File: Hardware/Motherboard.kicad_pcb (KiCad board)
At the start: 2 copper layers, 130 x 81.3 mm, 54 parts, among them J1 BME680, J2 JTAG, J3 Display_1, J4 Display_2, J5 Buttons, J6 USB, J7 MUSBD111M0_Supply, Q1 DMG3414U, SW1 Button_Plus, SW2 Button_Minus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

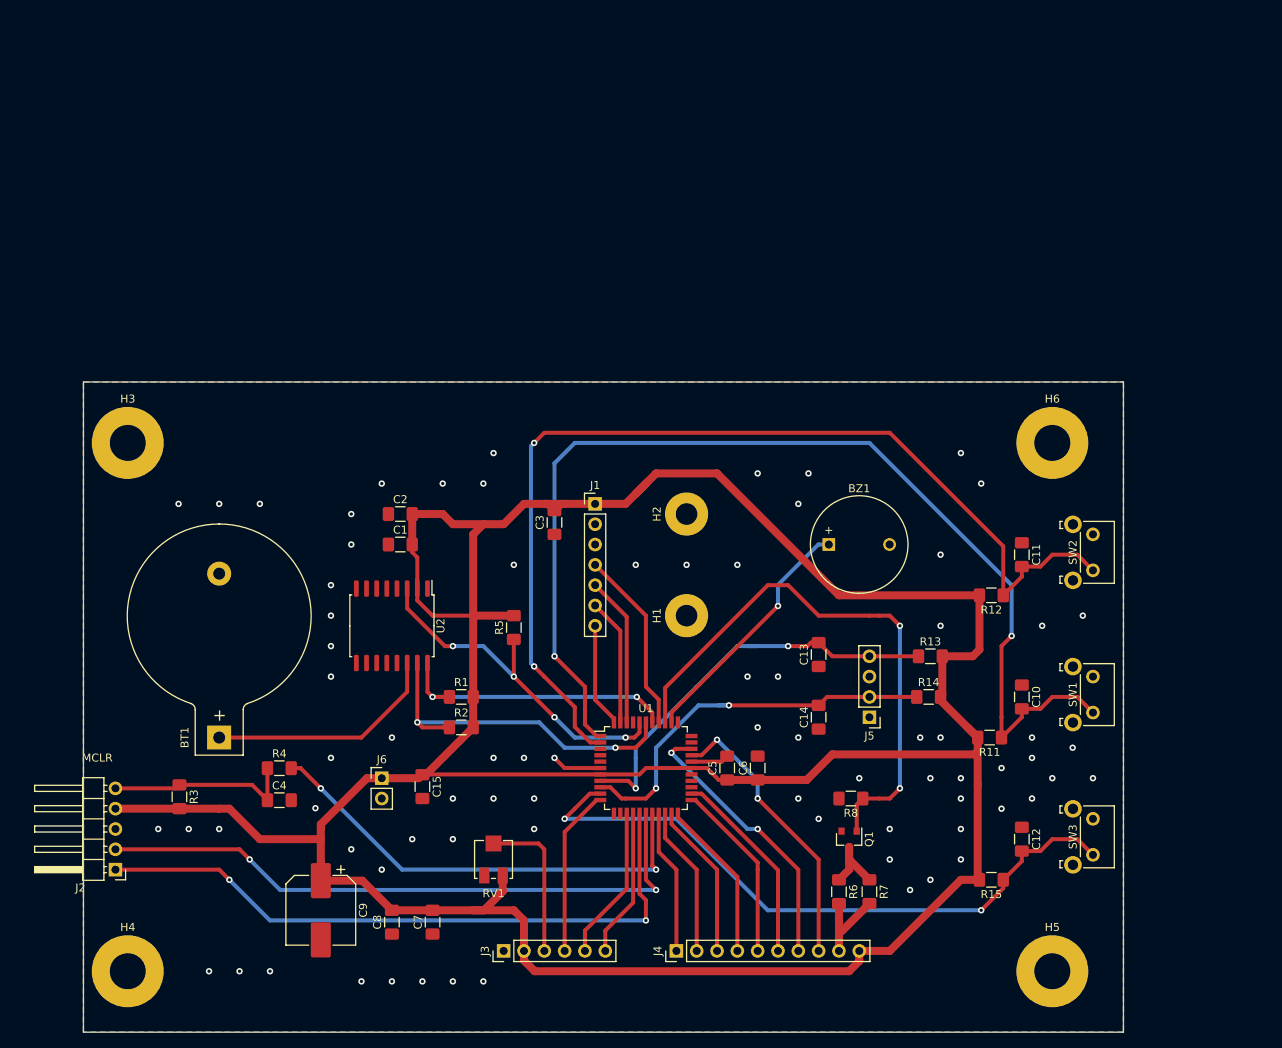
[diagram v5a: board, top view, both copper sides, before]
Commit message: [Hardware] Slightly decreased PCB height and adjusted it to millimeters.
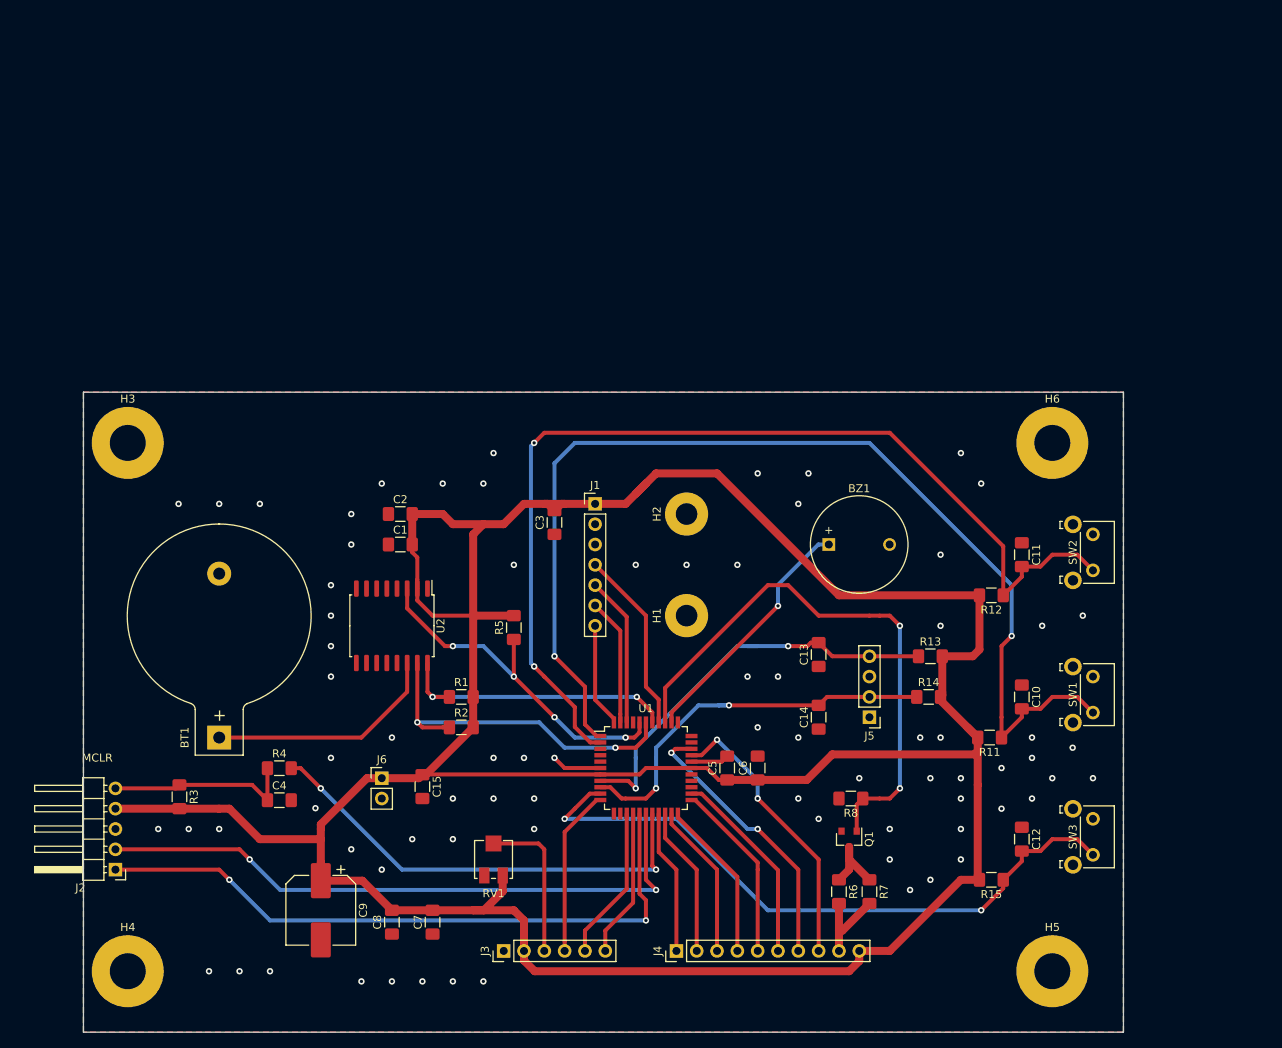
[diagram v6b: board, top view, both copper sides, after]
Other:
- board size 130 x 81.3 mm -> 130 x 80 mm
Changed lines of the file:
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@@
   (general
     (thickness 1.6)
-    (drawings 7)
+    (drawings 8)
     (tracks 463)
     (zones 0)
@@
     (solder_mask_min_width 0.25)
     (aux_axis_origin 0 0)
-    (grid_origin 234.95 134.62)
+    (grid_origin 104.95 134.62)
     (visible_elements FFFFFF7F)
     (pcbplotparams
@@
     )
   )
+  (dimension 80 (width 0.12) (layer F.SilkS)
+    (gr_text "80,000 mm" (at 91.68 94.62 90) (layer F.SilkS)
+      (effects (font (size 1 1) (thickness 0.15)))
+    )
+    (feature1 (pts (xy 104.95 54.62) (xy 92.363579 54.62)))
+    (feature2 (pts (xy 104.95 134.62) (xy 92.363579 134.62)))
+    (crossbar (pts (xy 92.95 134.62) (xy 92.95 54.62)))
+    (arrow1a (pts (xy 92.95 54.62) (xy 93.536421 55.746504)))
+    (arrow1b (pts (xy 92.95 54.62) (xy 92.363579 55.746504)))
+    (arrow2a (pts (xy 92.95 134.62) (xy 93.536421 133.493496)))
+    (arrow2b (pts (xy 92.95 134.62) (xy 92.363579 133.493496)))
+  )
   (dimension 130 (width 0.12) (layer F.SilkS)
     (gr_text "130,000 mm" (at 169.95 139.89) (layer F.SilkS)
@@
     (effects (font (size 1 1) (thickness 0.15)))
   )
-  (gr_line (start 104.95 53.34) (end 234.95 53.34) (layer Edge.Cuts) (width 0.05))
-  (gr_line (start 104.95 134.62) (end 104.95 53.34) (layer Edge.Cuts) (width 0.05))
+  (gr_line (start 104.95 54.62) (end 234.95 54.62) (layer Edge.Cuts) (width 0.05))
+  (gr_line (start 104.95 134.62) (end 104.95 54.62) (layer Edge.Cuts) (width 0.05))
   (gr_line (start 234.95 134.62) (end 104.95 134.62) (layer Edge.Cuts) (width 0.05))
-  (gr_line (start 234.95 53.34) (end 234.95 134.62) (layer Edge.Cuts) (width 0.05))
+  (gr_line (start 234.95 54.62) (end 234.95 134.62) (layer Edge.Cuts) (width 0.05))
   (segment (start 157.48 71.12) (end 160.02 68.58) (width 1) (layer F.Cu) (net 1))
   (segment (start 149.86 69.85) (end 151.13 71.12) (width 1) (layer F.Cu) (net 1))
@@
     (polygon
       (pts
-        (xy 104.95 53.34) (xy 234.95 53.34) (xy 234.95 134.62) (xy 104.95 134.62)
+        (xy 104.95 54.62) (xy 234.95 54.62) (xy 234.95 134.62) (xy 104.95 134.62)
       )
     )
@@
     (polygon
       (pts
-        (xy 104.95 53.34) (xy 234.95 53.34) (xy 234.95 134.62) (xy 104.95 134.62)
+        (xy 104.95 54.62) (xy 234.95 54.62) (xy 234.95 134.62) (xy 104.95 134.62)
       )
     )

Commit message: [Hardware] Moved PCB mounting holes to fit new board dimensions.
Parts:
- moved H3 2.97 mm to (113.0, 62.6)
- moved H4 2.49 mm to (113.0, 126.6)
- moved SW2 2.23 mm to (231.1, 74.6)
- moved H6 1.88 mm to (226.9, 62.6)
- moved SW1 1.45 mm to (231.1, 91.6)
- moved H5 0.97 mm to (226.9, 126.6)
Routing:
- net /PLUS_BUTTON: track 136.8 -> 136.2 mm
- net GND: vias 77 -> 81
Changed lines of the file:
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@@
   )
   (module MountingHole:MountingHole_4.5mm_Pad (layer F.Cu)
-    (at 226.06 60.96)
+    (at 226.95 62.62)
     (descr "Mounting Hole 4.5mm")
     (tags "mounting hole 4.5mm")
@@
   )
   (module MountingHole:MountingHole_4.5mm_Pad (layer F.Cu)
-    (at 226.06 127)
+    (at 226.95 126.62)
     (descr "Mounting Hole 4.5mm")
     (tags "mounting hole 4.5mm")
@@
   )
   (module MountingHole:MountingHole_4.5mm_Pad (layer F.Cu)
-    (at 110.49 127)
+    (at 112.95 126.62)
     (descr "Mounting Hole 4.5mm")
     (tags "mounting hole 4.5mm")
@@
   )
   (module MountingHole:MountingHole_4.5mm_Pad (layer F.Cu)
-    (at 110.49 60.96)
+    (at 112.95 62.62)
     (descr "Mounting Hole 4.5mm")
     (tags "mounting hole 4.5mm")
@@
   )
   (module Button_Switch_THT:SW_Tactile_SKHH_Angled (layer F.Cu)
-    (at 231.14 90.17 270)
+    (at 231.14 91.62 270)
     (descr "tactile switch 6mm ALPS SKHH right angle http://www.alps.com/prod/info/E/HTML/Tact/SnapIn/SKHH/SKHHLUA010.html")
     (tags "tactile switch 6mm ALPS SKHH right angle")
@@
   )
   (module Button_Switch_THT:SW_Tactile_SKHH_Angled (layer F.Cu)
-    (at 231.14 72.39 270)
+    (at 231.14 74.62 270)
     (descr "tactile switch 6mm ALPS SKHH right angle http://www.alps.com/prod/info/E/HTML/Tact/SnapIn/SKHH/SKHHLUA010.html")
     (tags "tactile switch 6mm ALPS SKHH right angle")
@@
   (via (at 205.74 113.03) (size 0.8) (drill 0.4) (layers F.Cu B.Cu) (net 2))
   (via (at 205.74 109.22) (size 0.8) (drill 0.4) (layers F.Cu B.Cu) (net 2))
-  (via (at 219.71 101.6) (size 0.8) (drill 0.4) (layers F.Cu B.Cu) (net 2))
-  (via (at 223.52 100.33) (size 0.8) (drill 0.4) (layers F.Cu B.Cu) (net 2))
-  (via (at 223.52 97.79) (size 0.8) (drill 0.4) (layers F.Cu B.Cu) (net 2))
-  (via (at 228.6 99.06) (size 0.8) (drill 0.4) (layers F.Cu B.Cu) (net 2))
-  (via (at 226.06 102.87) (size 0.8) (drill 0.4) (layers F.Cu B.Cu) (net 2))
-  (via (at 223.52 105.41) (size 0.8) (drill 0.4) (layers F.Cu B.Cu) (net 2))
-  (via (at 219.71 106.68) (size 0.8) (drill 0.4) (layers F.Cu B.Cu) (net 2))
+  (via (at 231.442 71.628) (size 0.8) (drill 0.4) (layers F.Cu B.Cu) (net 2))
+  (via (at 228.394 71.12) (size 0.8) (drill 0.4) (layers F.Cu B.Cu) (net 2))
+  (via (at 222.298 88.9) (size 0.8) (drill 0.4) (layers F.Cu B.Cu) (net 2))
+  (via (at 228.394 100.076) (size 0.8) (drill 0.4) (layers F.Cu B.Cu) (net 2))
+  (via (at 222.298 106.68) (size 0.8) (drill 0.4) (layers F.Cu B.Cu) (net 2))
+  (via (at 231.442 105.156) (size 0.8) (drill 0.4) (layers F.Cu B.Cu) (net 2))
+  (via (at 228.394 104.14) (size 0.8) (drill 0.4) (layers F.Cu B.Cu) (net 2))
   (via (at 212.09 97.79) (size 0.8) (drill 0.4) (layers F.Cu B.Cu) (net 2))
   (via (at 209.55 97.79) (size 0.8) (drill 0.4) (layers F.Cu B.Cu) (net 2))
@@
   (via (at 191.77 90.17) (size 0.8) (drill 0.4) (layers F.Cu B.Cu) (net 2))
   (via (at 212.09 83.82) (size 0.8) (drill 0.4) (layers F.Cu B.Cu) (net 2))
-  (via (at 224.79 83.82) (size 0.8) (drill 0.4) (layers F.Cu B.Cu) (net 2))
-  (via (at 229.87 82.55) (size 0.8) (drill 0.4) (layers F.Cu B.Cu) (net 2))
+  (via (at 228.394 87.884) (size 0.8) (drill 0.4) (layers F.Cu B.Cu) (net 2))
+  (via (at 228.394 82.804) (size 0.8) (drill 0.4) (layers F.Cu B.Cu) (net 2))
   (via (at 214.63 62.23) (size 0.8) (drill 0.4) (layers F.Cu B.Cu) (net 2))
   (via (at 217.17 66.04) (size 0.8) (drill 0.4) (layers F.Cu B.Cu) (net 2))
@@
   (via (at 127 68.58) (size 0.8) (drill 0.4) (layers F.Cu B.Cu) (net 2))
   (via (at 121.92 68.58) (size 0.8) (drill 0.4) (layers F.Cu B.Cu) (net 2))
-  (via (at 116.84 68.58) (size 0.8) (drill 0.4) (layers F.Cu B.Cu) (net 2))
+  (via (at 121.95 64.62) (size 0.8) (drill 0.4) (layers F.Cu B.Cu) (net 2))
   (via (at 135.89 78.74) (size 0.8) (drill 0.4) (layers F.Cu B.Cu) (net 2))
   (via (at 135.89 82.55) (size 0.8) (drill 0.4) (layers F.Cu B.Cu) (net 2))
@@
   (segment (start 184.7325 100.8) (end 185.42 100.1125) (width 0.5) (layer F.Cu) (net 2))
   (segment (start 180.96 100.8) (end 184.7325 100.8) (width 0.5) (layer F.Cu) (net 2))
-  (via (at 231.14 102.87) (size 0.8) (drill 0.4) (layers F.Cu B.Cu) (net 2))
+  (via (at 231.14 88.9) (size 0.8) (drill 0.4) (layers F.Cu B.Cu) (net 2))
   (via (at 138.43 111.76) (size 0.8) (drill 0.4) (layers F.Cu B.Cu) (net 2))
   (via (at 142.24 114.3) (size 0.8) (drill 0.4) (layers F.Cu B.Cu) (net 2))
@@
   (via (at 118.11 109.22) (size 0.8) (drill 0.4) (layers F.Cu B.Cu) (net 2))
   (via (at 133.95 106.62) (size 0.8) (drill 0.4) (layers F.Cu B.Cu) (net 2))
+  (via (at 126.95 64.62) (size 0.8) (drill 0.4) (layers F.Cu B.Cu) (net 2))
+  (via (at 218.95 124.62) (size 0.8) (drill 0.4) (layers F.Cu B.Cu) (net 2))
+  (via (at 218.95 127.62) (size 0.8) (drill 0.4) (layers F.Cu B.Cu) (net 2))
+  (via (at 218.95 130.62) (size 0.8) (drill 0.4) (layers F.Cu B.Cu) (net 2))
   (segment (start 168.91 83.82) (end 168.91 93.075) (width 0.5) (layer F.Cu) (net 3))
   (segment (start 171.26 95.425) (end 171.26 95.9) (width 0.5) (layer F.Cu) (net 3))
@@
   (segment (start 161.83 111.03) (end 162.56 111.76) (width 0.5) (layer F.Cu) (net 44))
   (segment (start 169.56 97.6) (end 169.1 97.6) (width 0.5) (layer F.Cu) (net 47))
-  (segment (start 222.25 94.1975) (end 224.5725 94.1975) (width 0.5) (layer F.Cu) (net 47))
-  (segment (start 224.5725 94.1975) (end 226.06 92.71) (width 0.5) (layer F.Cu) (net 47))
-  (segment (start 229.18 92.71) (end 231.14 94.67) (width 0.5) (layer F.Cu) (net 47))
-  (segment (start 226.06 92.71) (end 229.18 92.71) (width 0.5) (layer F.Cu) (net 47))
   (segment (start 222.25 95.25) (end 219.71 97.79) (width 0.5) (layer F.Cu) (net 47))
   (segment (start 222.25 94.1975) (end 222.25 95.25) (width 0.5) (layer F.Cu) (net 47))
@@
   (segment (start 163.83 87.63) (end 163.83 63.5) (width 0.5) (layer B.Cu) (net 47))
   (segment (start 163.83 63.5) (end 166.37 60.96) (width 0.5) (layer B.Cu) (net 47))
-  (segment (start 222.25 76.4175) (end 224.5725 76.4175) (width 0.5) (layer F.Cu) (net 48))
-  (segment (start 224.5725 76.4175) (end 226.06 74.93) (width 0.5) (layer F.Cu) (net 48))
-  (segment (start 229.18 74.93) (end 231.14 76.89) (width 0.5) (layer F.Cu) (net 48))
-  (segment (start 226.06 74.93) (end 229.18 74.93) (width 0.5) (layer F.Cu) (net 48))
+  (segment (start 229.2175 94.1975) (end 222.25 94.1975) (width 0.5) (layer F.Cu) (net 47))
+  (segment (start 231.14 96.12) (end 229.2175 94.1975) (width 0.5) (layer F.Cu) (net 47))
   (segment (start 222.25 77.6875) (end 219.9275 80.01) (width 0.5) (layer F.Cu) (net 48))
   (segment (start 222.25 76.4175) (end 222.25 77.6875) (width 0.5) (layer F.Cu) (net 48))
@@
   (segment (start 160.890001 61.359999) (end 160.890001 88.500001) (width 0.5) (layer B.Cu) (net 48))
   (segment (start 161.29 60.96) (end 160.890001 61.359999) (width 0.5) (layer B.Cu) (net 48))
+  (segment (start 228.4375 76.4175) (end 222.25 76.4175) (width 0.5) (layer F.Cu) (net 48))
+  (segment (start 231.14 79.12) (end 228.4375 76.4175) (width 0.5) (layer F.Cu) (net 48))
   (segment (start 175.26 107.3) (end 175.26 115.57) (width 0.5) (layer F.Cu) (net 49))
   (segment (start 175.26 115.57) (end 176.53 116.84) (width 0.5) (layer F.Cu) (net 49))

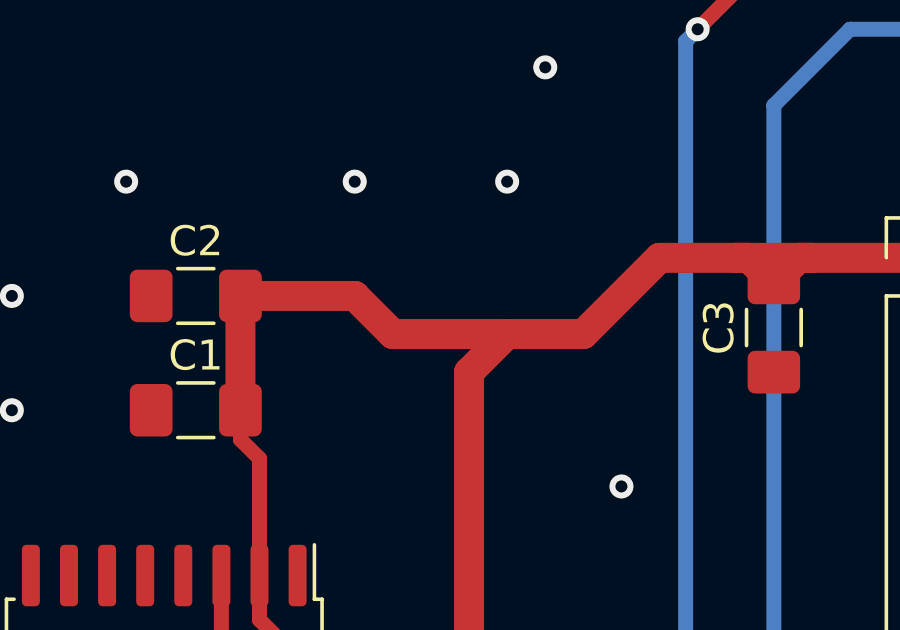
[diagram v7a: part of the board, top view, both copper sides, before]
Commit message: [Hardware] Added PCB switches 3D model.
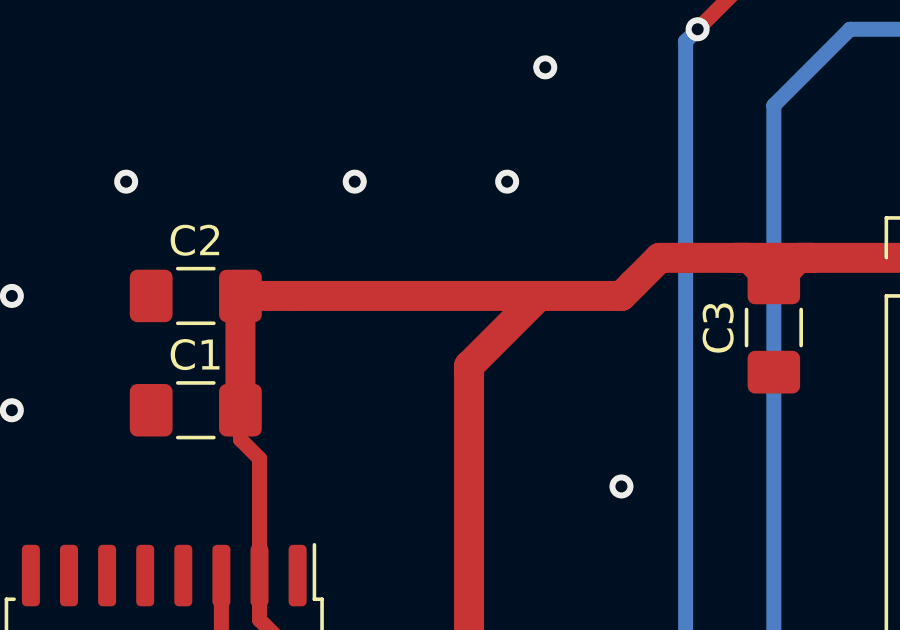
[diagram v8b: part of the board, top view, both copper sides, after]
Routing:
- net +5V: track 411.2 -> 411.8 mm
